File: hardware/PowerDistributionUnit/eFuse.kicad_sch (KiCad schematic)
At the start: 26 parts, among them Q19 CSD18511Q5A, U4 AD5258, U5 TPS25983

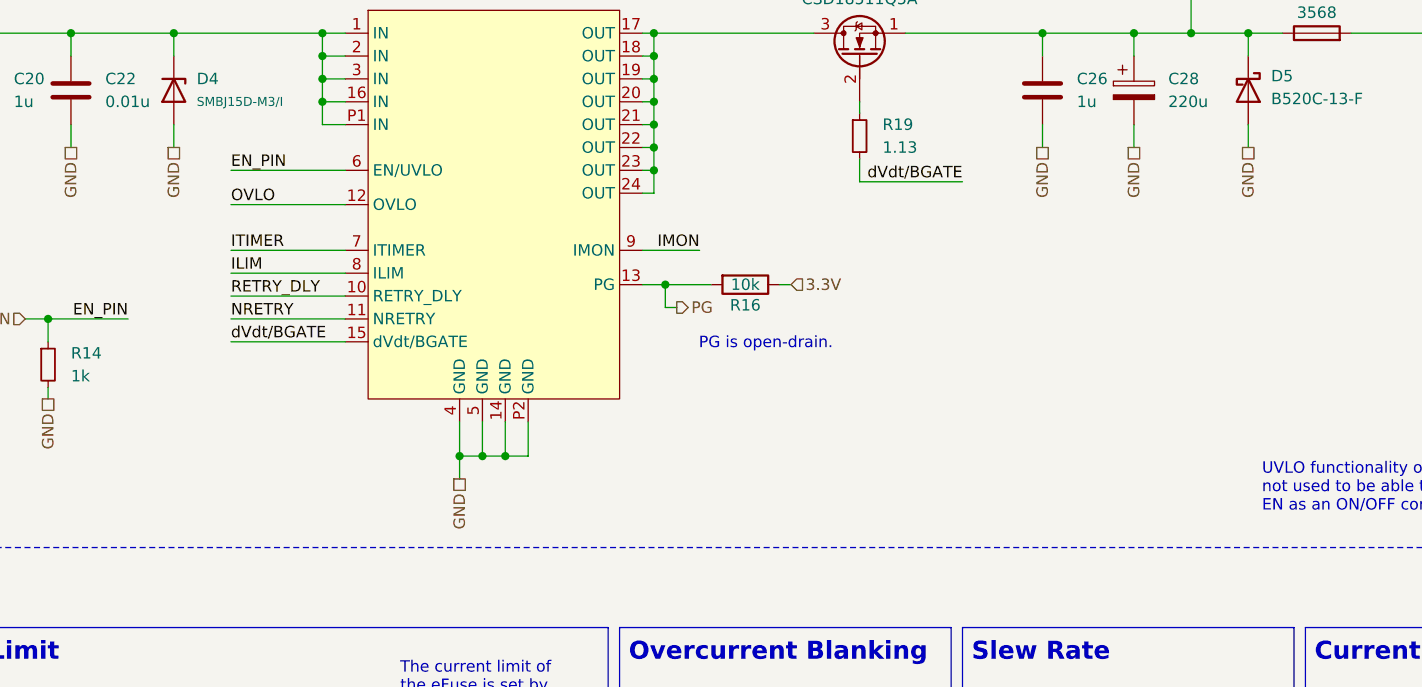
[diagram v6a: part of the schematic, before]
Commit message: added gndpwr to separate from everything on gnd
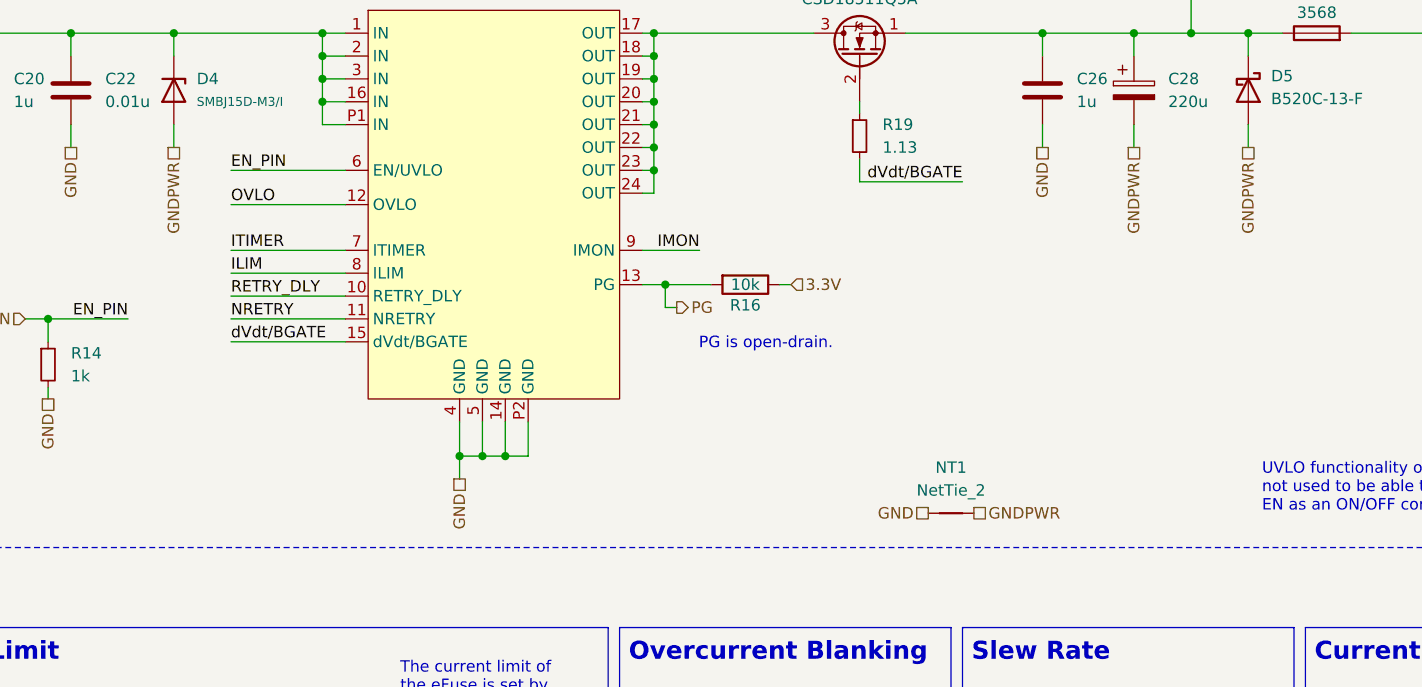
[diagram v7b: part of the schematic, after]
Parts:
- added NT1: NetTie_2, symbol Device:NetTie_2
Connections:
- net GND: now also NT1.1; no longer C28.2, D4.2 (A), D5.2 (A)
- new net GNDPWR: C28.2, D4.2 (A), D5.2 (A), NT1.2
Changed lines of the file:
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@@
+		)
+	)
+	(hierarchical_label "GND"
+		(shape passive)
+		(at 135.89 87.63 180)
+		(fields_autoplaced yes)
+		(effects
+			(font
+				(size 1.27 1.27)
+				(color 0 0 0 1)
+			)
+			(justify right)
 		)
 	)
@@
 		)
 	)
-	(hierarchical_label "GND"
+	(hierarchical_label "GNDPWR"
 		(shape passive)
 		(at 52.07 46.99 270)
@@
 		)
 	)
-	(hierarchical_label "GND"
+	(hierarchical_label "GNDPWR"
 		(shape passive)
 		(at 171.45 46.99 270)
@@
 		)
 	)
+	(hierarchical_label "GNDPWR"
+		(shape passive)
+		(at 140.97 87.63 0)
+		(fields_autoplaced yes)
+		(effects
+			(font
+				(size 1.27 1.27)
+				(color 0 0 0 1)
+			)
+			(justify left)
+		)
+	)
 	(hierarchical_label "GND"
 		(shape passive)
@@
 		)
 	)
-	(hierarchical_label "GND"
+	(hierarchical_label "GNDPWR"
 		(shape passive)
 		(at 158.75 46.99 270)
@@
 					(unit 1)
 				)
+			)
+		)
+	)
+	(symbol
+		(lib_id "Device:NetTie_2")
+		(at 138.43 87.63 0)
+		(unit 1)
+		(exclude_from_sim no)
+		(in_bom no)
+		(on_board yes)
+		(dnp no)
+		(fields_autoplaced yes)
+		(property "Reference" "NT1"
+			(at 138.43 82.55 0)
+			(effects
+				(font
+					(size 1.27 1.27)
+				)
+			)
+		)
+		(property "Value" "NetTie_2"
+			(at 138.43 85.09 0)
+			(effects
+				(font
+					(size 1.27 1.27)
+				)
+			)
+		)
+		(property "Footprint" ""
+			(at 138.43 87.63 0)
+			(effects
+				(font
+					(size 1.27 1.27)
+				)
+				(hide yes)
+			)
+		)
+		(property "Datasheet" "~"
+			(at 138.43 87.63 0)
+			(effects
+				(font
+					(size 1.27 1.27)
+				)
+				(hide yes)
+			)
+		)
+		(property "Description" "Net tie, 2 pins"
+			(at 138.43 87.63 0)
+			(effects
+				(font
+					(size 1.27 1.27)
+				)
+				(hide yes)
+			)
+		)
+		(pin "1"
+		)
+		(pin "2"
+		)
+		(instances
+			(project ""
+				(path "/93fa4ef0-f02c-4535-aca9-c62461ff58dd/afc26468-877c-4928-9f2e-9c48c52cd2d4/12f77c20-05fa-4d9c-aec3-c07e18b6d94a"
+					(reference "NT3")
+					(unit 1)
+				)
+				(path "/93fa4ef0-f02c-4535-aca9-c62461ff58dd/afc26468-877c-4928-9f2e-9c48c52cd2d4/1f358fa3-a889-4029-906a-d24c77ca2d2c"
+					(reference "NT12")
+					(unit 1)
+				)
+				(path "/93fa4ef0-f02c-4535-aca9-c62461ff58dd/afc26468-877c-4928-9f2e-9c48c52cd2d4/215c0e10-1c35-49de-82cd-ab2f3dd12a9e"
+					(reference "NT1")
+					(unit 1)
+				)
+				(path "/93fa4ef0-f02c-4535-aca9-c62461ff58dd/afc26468-877c-4928-9f2e-9c48c52cd2d4/45080e39-d0e0-46fa-9a7d-dc213e062091"
+					(reference "NT10")
+					(unit 1)
+				)
+				(path "/93fa4ef0-f02c-4535-aca9-c62461ff58dd/afc26468-877c-4928-9f2e-9c48c52cd2d4/4fe7e578-4c31-4362-b2ce-382c78313084"
+					(reference "NT8")
+					(unit 1)
+				)
+				(path "/93fa4ef0-f02c-4535-aca9-c62461ff58dd/afc26468-877c-4928-9f2e-9c48c52cd2d4/62a8656a-3368-4168-badf-be5ed339c086"
+					(reference "NT2")
+					(unit 1)
+				)
+				(path "/93fa4ef0-f02c-4535-aca9-c62461ff58dd/afc26468-877c-4928-9f2e-9c48c52cd2d4/6be26867-cff6-432f-8722-bbdff7bef258"
+					(reference "NT5")
+					(unit 1)
+				)
+				(path "/93fa4ef0-f02c-4535-aca9-c62461ff58dd/afc26468-877c-4928-9f2e-9c48c52cd2d4/81b4a052-923b-40a7-96aa-a0588ccb881f"
+					(reference "NT6")
+					(unit 1)
+				)
+				(path "/93fa4ef0-f02c-4535-aca9-c62461ff58dd/afc26468-877c-4928-9f2e-9c48c52cd2d4/8c872111-9b56-46eb-86fe-f81e0a1b0aea"
+					(reference "NT4")
+					(unit 1)
+				)
+				(path "/93fa4ef0-f02c-4535-aca9-c62461ff58dd/afc26468-877c-4928-9f2e-9c48c52cd2d4/ac9891f9-3fa8-47a7-ac15-e6baf4318520"
+					(reference "NT7")
+					(unit 1)
+				)
+				(path "/93fa4ef0-f02c-4535-aca9-c62461ff58dd/afc26468-877c-4928-9f2e-9c48c52cd2d4/b137fa60-d290-4b94-9988-a3f6fdf61279"
+					(reference "NT11")
+					(unit 1)
+				)
+				(path "/93fa4ef0-f02c-4535-aca9-c62461ff58dd/afc26468-877c-4928-9f2e-9c48c52cd2d4/cf101698-6453-4dc2-945c-b3975bb3daa4"
+					(reference "NT9")
+					(unit 1)
+				)
+				(path "/93fa4ef0-f02c-4535-aca9-c62461ff58dd/afc26468-877c-4928-9f2e-9c48c52cd2d4/ee1e7bb5-535f-47d5-bf1b-6e8da704ac91"
+					(reference "NT15")
+					(unit 1)
+				)
+				(path "/93fa4ef0-f02c-4535-aca9-c62461ff58dd/afc26468-877c-4928-9f2e-9c48c52cd2d4/f45b2dad-2c26-41bf-871e-7a4a557a3789"
+					(reference "NT14")
+					(unit 1)
+				)
+				(path "/93fa4ef0-f02c-4535-aca9-c62461ff58dd/afc26468-877c-4928-9f2e-9c48c52cd2d4/f7e10137-69e0-480a-8df5-8d0dccdcc2d2"
+					(reference "NT13")
+					(unit 1)
+				)

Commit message: schematic updated
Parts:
- removed D4: SMBJ15D-M3/I, Diode_SMD:D_SMB, symbol Device:D_Zener
- added D1: LED, LED_SMD:LED_0805_2012Metric, symbol Device:LED
- added D49: SMF15A-HE3-08, Diode_SMD:D_SMF, symbol Device:D_Zener
- added Q2: 2N7002, Package_TO_SOT_SMD:SOT-23, symbol Transistor_FET:Q_NMOS_GSD
- added R143: R, Resistor_SMD:R_0603_1608Metric, symbol Device:R
- added R145: 10k, Resistor_SMD:R_0603_1608Metric, symbol Device:R_Small
- added R146: 1k, Resistor_SMD:R_0603_1608Metric, symbol Device:R_Small
- added R221: 110k, Resistor_SMD:R_0603_1608Metric, symbol Device:R
- added TP110, TP126, TP14, TP142, TP158, TP174, TP190, TP206, TP222, TP78, TP94: TestPoint, TestPoint:TestPoint_Pad_D1.0mm, symbol Connector:TestPoint
- added TP238: TestPoint, Connector_PinHeader_2.54mm:PinHeader_1x01_P2.54mm_Vertical, symbol Connector:TestPoint
- C11: renamed from C25; value C -> 220p; footprint (none) -> Capacitor_SMD:C_0603_1608Metric; now fitted
- C2: renamed from C19; value C -> 220n; footprint (none) -> Capacitor_SMD:C_0603_1608Metric; now fitted
- C3: renamed from C20; footprint (none) -> Capacitor_SMD:C_0603_1608Metric
- C4: renamed from C21; footprint (none) -> Capacitor_SMD:C_0603_1608Metric
- C5: renamed from C22; footprint (none) -> Capacitor_SMD:C_0603_1608Metric
- C6: renamed from C23; footprint (none) -> Capacitor_SMD:C_0603_1608Metric
- C63: renamed from C26; footprint (none) -> Capacitor_SMD:C_0603_1608Metric
- C64: renamed from C27; value C -> 3n; footprint (none) -> Capacitor_SMD:C_0603_1608Metric; now fitted
- C65: renamed from C28; value 220u -> 47u; footprint Capacitor_SMD:CP_Elec_10x10.5 -> Capacitor_SMD:CP_Elec_6.3x4.9
- C66: renamed from C29; value 1u -> 0.1n; footprint (none) -> Capacitor_SMD:C_0603_1608Metric; symbol Device:C -> Device:C_Small
- C7: renamed from C24; footprint (none) -> Capacitor_SMD:C_0603_1608Metric
- D12: renamed from D5; value B520C-13-F -> PMEG6030AEXEX; footprint Diode_SMD:D_SMC -> PowerDistributionUnitLib:PMEG4030AEXEQX; Link (none) -> https://www.mouser.com/ProductDetail/Nexperia/PMEG6030AEXEX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
- NT1: footprint (none) -> NetTie:NetTie-2_SMD_Pad0.5mm
- R148: renamed from R150; footprint (none) -> Resistor_SMD:R_0603_1608Metric
- R2: renamed from R13; footprint (none) -> Resistor_SMD:R_0603_1608Metric
- R3: renamed from R14; value 1k -> 1M; footprint (none) -> Resistor_SMD:R_0603_1608Metric; symbol Device:R_Small -> Device:R
- R45: renamed from R17; value 972k -> 1M; footprint (none) -> Resistor_SMD:R_0603_1608Metric
- R46: renamed from R18; value 102k -> 88.7k; footprint (none) -> Resistor_SMD:R_0603_1608Metric
- R47: renamed from R19; footprint (none) -> Resistor_SMD:R_0603_1608Metric
- R48: renamed from R20; value 549 -> 681; footprint (none) -> Resistor_SMD:R_0603_1608Metric
- R5: renamed from R15; footprint (none) -> Resistor_SMD:R_0603_1608Metric
- R8: renamed from R16; footprint (none) -> Resistor_SMD:R_0603_1608Metric
- renumbered F2 to F6, Q19 to Q1, U4 to U12, U5 to U13
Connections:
- net 3.3V: now also D1.2 (A)
- net EN: now also R3.2, R221.1, TP142.1; no longer R3.1
- net GND: now also Q2.2 (S), R143.2, R221.2; no longer R3.2
- net GNDPWR: now also D49.2 (A)
- net ILIM: now also R143.1, TP190.1
- net IMON: now also R145.2, TP110.1; no longer C66.1, R48.1, U13.9 (IMON)
- net IN: now also R3.1, D49.1 (K)
- net ITIMER: now also TP174.1
- net NRETRY: now also TP222.1
- net OUT: now also TP238.1
- net OVLO: now also TP158.1
- net PG: now also Q2.1 (G), TP126.1
- net RETRY_DLY: now also TP206.1
- net dVdt/BGATE: now also TP94.1
- net EFET_OUT: now reaches C63.1, C65.1, D12.1 (K), F6.1, Q1.1 (S), R148.2
- net EFET_OUT: now also TP14.1
- net EFUSE_OUT: now reaches Q1.3 (D), U13.17 (OUT), U13.18 (OUT), U13.19 (OUT), U13.20 (OUT), U13.21 (OUT), U13.22 (OUT), U13.23 (OUT), U13.24 (OUT)
- net EFUSE_OUT: now also TP78.1
- new net: D1.1 (K), R146.1
- new net: Q2.3 (D), R146.2
- new net IMON_PIN: C66.1, R145.1, R48.1, U13.9 (IMON)
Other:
- note added: "ADJUSTABLE LIMIT"
- note added: "FIXED LIMIT"
- note added: "OVLO & UVLO/EN"
- note added: "PG Indicator"
- note added: "Test Points"
- note removed: "Overvoltage Lockout"
- note removed: "UVLO functionality of eFuse not used to be able to use EN as an ON/OFF control."
- company: (none) -> Longhorn Racing Solar
- title: (none) -> eFuse Output X
- moved on the sheet: C4, C6, C63, C65, C66, C7, D12, F6, NT1, Q1, R148, R2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
